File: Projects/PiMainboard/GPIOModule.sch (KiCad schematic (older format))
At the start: 0 parts

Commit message: Added lots more to modules!
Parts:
- added C1_G: 2.2pF, symbol cap_np
- added C2_G: 10pF, symbol cap_np
- added J1_G, J2_G, J3_G, J4_G: HEADER_4, symbol HEADER_4
- added J5_G: HEADER_6, symbol HEADER_6
- added R1_G, R2_G, R3_G, R4_G: 1k8, symbol R
- added R5_G: 1k, symbol R
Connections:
- net FM: now also C1_G.1, C2_G.1
- net GPIO17: now also J5_G.1
- net GPIO22: now also J5_G.2
- net GPIO23: now also J5_G.3
- net GPIO24: now also J5_G.4
- net PWM: now also J5_G.5
- net SCL: now also J1_G.2, J2_G.2, R2_G.2, R4_G.2
- net SDA: now also J1_G.1, J2_G.1, R1_G.2, R3_G.2
- net UART_RX0: now also J3_G.2
- net UART_RX1: now also J4_G.2
- net UART_TX0: now also J3_G.1
- net UART_TX1: now also J4_G.1
- new net: C1_G.2, J5_G.6, R5_G.1
- new net: C2_G.2, R5_G.2
- new net 3v3: J1_G.4, J2_G.4, J3_G.4, J4_G.4, R1_G.1, R2_G.1, R3_G.1, R4_G.1
- new net GND: J1_G.3, J2_G.3, J3_G.3, J4_G.3

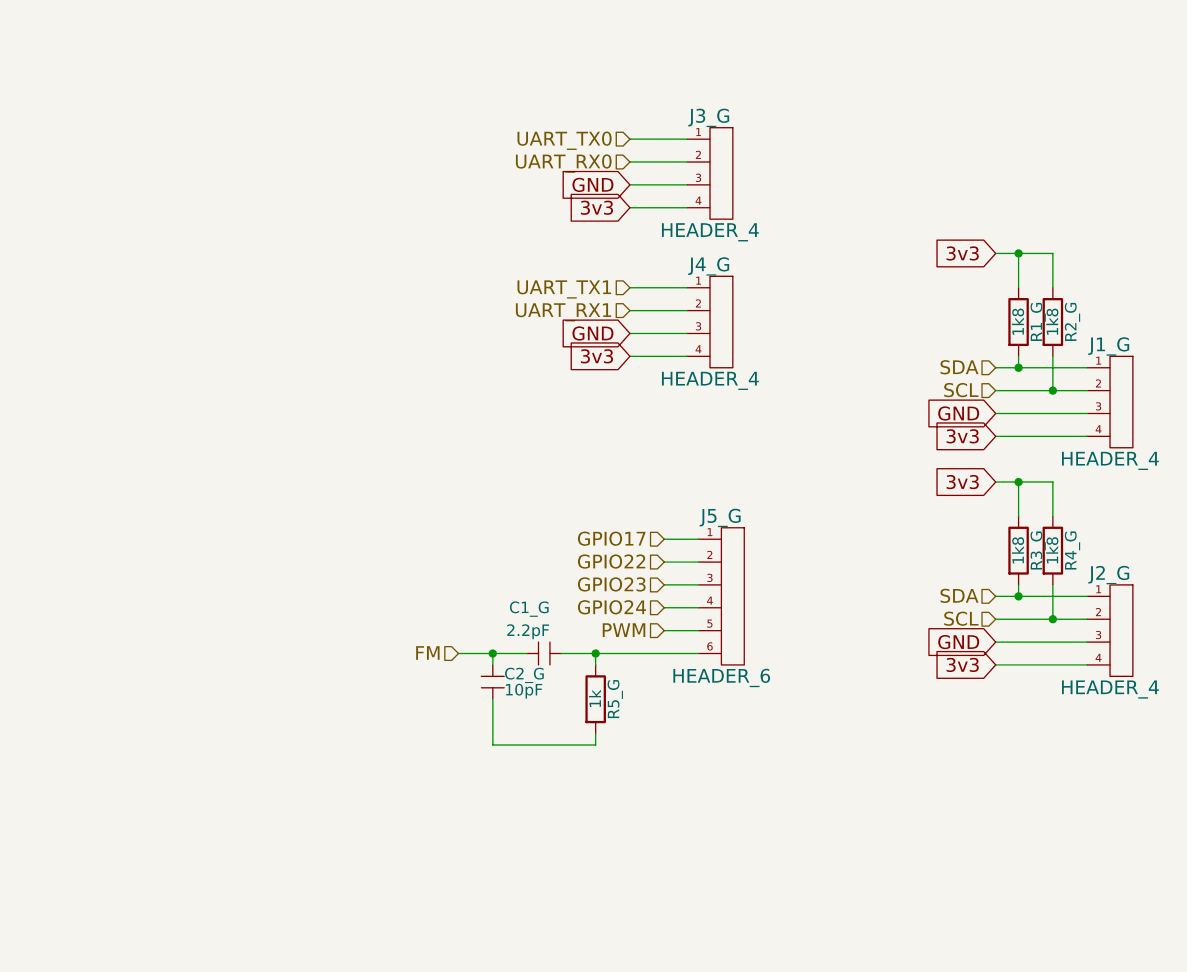
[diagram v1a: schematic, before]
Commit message: Added PI CM IO "shield"
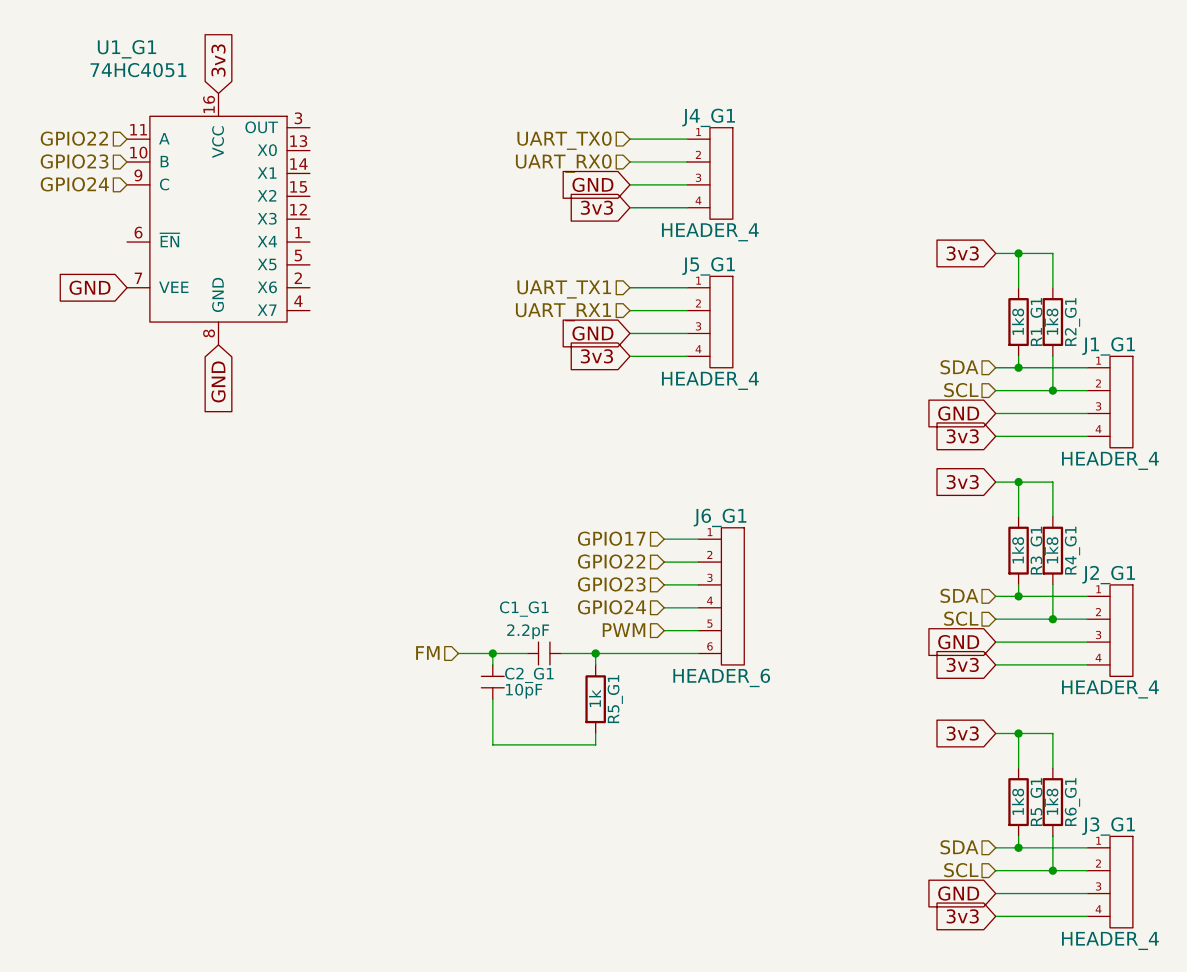
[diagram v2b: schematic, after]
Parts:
- added J3_G1: HEADER_4, symbol HEADER_4
- added R5_G1, R6_G1: 1k8, symbol R
- added U1_G1: 74HC4051, symbol 74HC4051
- renumbered C1_G to C1_G1, C2_G to C2_G1, J1_G to J1_G1, J2_G to J2_G1, J3_G to J3_G1, J4_G to J4_G1, J5_G to J5_G1, R1_G to R1_G1, R2_G to R2_G1, R3_G to R3_G1, R4_G to R4_G1, R5_G to R5_G1
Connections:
- net 3v3: now also J3_G1.4, R5_G1.1, R6_G1.1, U1_G1.16 (VCC)
- net GND: now also J3_G1.3, U1_G1.7 (VEE), U1_G1.8 (GND)
- net GPIO22: now also U1_G1.11 (A)
- net GPIO23: now also U1_G1.10 (B)
- net GPIO24: now also U1_G1.9 (C)
- net SCL: now also J3_G1.2, R6_G1.2
- net SDA: now also J3_G1.1, R5_G1.2
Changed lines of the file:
@@
 $Descr A4 11693 8268
 encoding utf-8
-Sheet 4 7
+Sheet 10 10
 Title ""
 Date ""
@@
 FM
 $Comp
-L HEADER_4 J1_G
+L HEADER_4 J1_G1
 U 1 1 5692992D
 P 6850 3000
-F 0 "J1_G" H 6850 3250 60  0000 C CNN
+AR Path="/5671AC37/5692992D" Ref="J1_G1"  Part="1"
+AR Path="/56EDDFF0/56EF4FDE/5692992D" Ref="J1_G1"  Part="1"
+F 0 "J1_G1" H 6850 3250 60  0000 C CNN
 F 1 "HEADER_4" H 6850 2750 60  0000 C CNN
 F 2 "" H 6850 3000 60  0000 C CNN
@@
 $EndComp
 $Comp
-L R R1_G
+L R R1_G1
 U 1 1 56929B23
 P 6450 2650
-F 0 "R1_G" V 6530 2650 50  0000 C CNN
+AR Path="/5671AC37/56929B23" Ref="R1_G1"  Part="1"
+AR Path="/56EDDFF0/56EF4FDE/56929B23" Ref="R1_G1"  Part="1"
+F 0 "R1_G1" V 6530 2650 50  0000 C CNN
 F 1 "1k8" V 6450 2650 50  0000 C CNN
 F 2 "" V 6380 2650 50  0000 C CNN
@@
 $EndComp
 $Comp
-L R R2_G
+L R R2_G1
 U 1 1 56929B6C
 P 6600 2650
-F 0 "R2_G" V 6680 2650 50  0000 C CNN
+AR Path="/5671AC37/56929B6C" Ref="R2_G1"  Part="1"
+AR Path="/56EDDFF0/56EF4FDE/56929B6C" Ref="R2_G1"  Part="1"
+F 0 "R2_G1" V 6680 2650 50  0000 C CNN
 F 1 "1k8" V 6600 2650 50  0000 C CNN
 F 2 "" V 6530 2650 50  0000 C CNN
@@
 SCL
 $Comp
-L HEADER_4 J2_G
+L HEADER_4 J2_G1
 U 1 1 56929E64
 P 6850 4000
-F 0 "J2_G" H 6850 4250 60  0000 C CNN
+AR Path="/5671AC37/56929E64" Ref="J2_G1"  Part="1"
+AR Path="/56EDDFF0/56EF4FDE/56929E64" Ref="J2_G1"  Part="1"
+F 0 "J2_G1" H 6850 4250 60  0000 C CNN
 F 1 "HEADER_4" H 6850 3750 60  0000 C CNN
 F 2 "" H 6850 4000 60  0000 C CNN
@@
 $EndComp
 $Comp
-L R R3_G
+L R R3_G1
 U 1 1 56929E6A
 P 6450 3650
-F 0 "R3_G" V 6530 3650 50  0000 C CNN
+AR Path="/5671AC37/56929E6A" Ref="R3_G1"  Part="1"
+AR Path="/56EDDFF0/56EF4FDE/56929E6A" Ref="R3_G1"  Part="1"
+F 0 "R3_G1" V 6530 3650 50  0000 C CNN
 F 1 "1k8" V 6450 3650 50  0000 C CNN
 F 2 "" V 6380 3650 50  0000 C CNN
@@
 $EndComp
 $Comp
-L R R4_G
+L R R4_G1
 U 1 1 56929E70
 P 6600 3650
-F 0 "R4_G" V 6680 3650 50  0000 C CNN
+AR Path="/5671AC37/56929E70" Ref="R4_G1"  Part="1"
+AR Path="/56EDDFF0/56EF4FDE/56929E70" Ref="R4_G1"  Part="1"
+F 0 "R4_G1" V 6680 3650 50  0000 C CNN
 F 1 "1k8" V 6600 3650 50  0000 C CNN
 F 2 "" V 6530 3650 50  0000 C CNN
@@
 3v3
 $Comp
-L HEADER_4 J3_G
+L HEADER_4 J3_G1
 U 1 1 5692A3DF
 P 5100 2000
-F 0 "J3_G" H 5100 2250 60  0000 C CNN
+AR Path="/5671AC37/5692A3DF" Ref="J3_G1"  Part="1"
+AR Path="/56EDDFF0/56EF4FDE/5692A3DF" Ref="J4_G1"  Part="1"
+F 0 "J4_G1" H 5100 2250 60  0000 C CNN
 F 1 "HEADER_4" H 5100 1750 60  0000 C CNN
 F 2 "" H 5100 2000 60  0000 C CNN
@@
 $EndComp
 $Comp
-L HEADER_4 J4_G
+L HEADER_4 J4_G1
 U 1 1 5692A48D
 P 5100 2650
-F 0 "J4_G" H 5100 2900 60  0000 C CNN
+AR Path="/5671AC37/5692A48D" Ref="J4_G1"  Part="1"
+AR Path="/56EDDFF0/56EF4FDE/5692A48D" Ref="J5_G1"  Part="1"
+F 0 "J5_G1" H 5100 2900 60  0000 C CNN
 F 1 "HEADER_4" H 5100 2400 60  0000 C CNN
 F 2 "" H 5100 2650 60  0000 C CNN
@@
 3v3
 $Comp
-L HEADER_6 J5_G
+L HEADER_6 J5_G1
 U 1 1 5692D1AF
 P 5150 3850
-F 0 "J5_G" H 5150 4200 60  0000 C CNN
+AR Path="/5671AC37/5692D1AF" Ref="J5_G1"  Part="1"
+AR Path="/56EDDFF0/56EF4FDE/5692D1AF" Ref="J6_G1"  Part="1"
+F 0 "J6_G1" H 5150 4200 60  0000 C CNN
 F 1 "HEADER_6" H 5150 3500 60  0000 C CNN
 F 2 "" H 5150 3850 60  0000 C CNN
@@
 $EndComp
 $Comp
-L cap_np C2_G
+L cap_np C2_G1
 U 1 1 5692D49F
 P 4150 4200
-F 0 "C2_G" H 4200 4210 50  0000 L CNN
+AR Path="/5671AC37/5692D49F" Ref="C2_G1"  Part="1"
+AR Path="/56EDDFF0/56EF4FDE/5692D49F" Ref="C2_G1"  Part="1"
+F 0 "C2_G1" H 4200 4210 50  0000 L CNN
 F 1 "10pF" H 4200 4140 50  0000 L CNN
 F 2 "" H 4150 4200 60  0000 C CNN
@@
 $EndComp
 $Comp
-L cap_np C1_G
+L cap_np C1_G1
 U 1 1 5692D596
 P 4350 4100
-F 0 "C1_G" V 4550 4050 50  0000 L CNN
+AR Path="/5671AC37/5692D596" Ref="C1_G1"  Part="1"
+AR Path="/56EDDFF0/56EF4FDE/5692D596" Ref="C1_G1"  Part="1"
+F 0 "C1_G1" V 4550 4050 50  0000 L CNN
 F 1 "2.2pF" V 4450 4050 50  0000 L CNN
 F 2 "" H 4350 4100 60  0000 C CNN
@@
 $EndComp
 $Comp
-L R R5_G
+L R R5_G1
 U 1 1 5692D5FB
 P 4600 4300
-F 0 "R5_G" V 4680 4300 50  0000 C CNN
+AR Path="/5671AC37/5692D5FB" Ref="R5_G1"  Part="1"
+AR Path="/56EDDFF0/56EF4FDE/5692D5FB" Ref="R5_G1"  Part="1"
+F 0 "R5_G1" V 4680 4300 50  0000 C CNN
 F 1 "1k" V 4600 4300 50  0000 C CNN
 F 2 "" V 4530 4300 50  0000 C CNN
@@
 Connection ~ 4150 4100
 Connection ~ 4600 4100
+Text HLabel 6350 4950 0    60   Input ~ 0
+SDA
+Text HLabel 6350 5050 0    60   Input ~ 0
+SCL
+$Comp
+L HEADER_4 J3_G1
+U 1 1 56EF8CFB
+P 6850 5100
+F 0 "J3_G1" H 6850 5350 60  0000 C CNN
+F 1 "HEADER_4" H 6850 4850 60  0000 C CNN
+F 2 "" H 6850 5100 60  0000 C CNN
+F 3 "" H 6850 5100 60  0000 C CNN
+	1    6850 5100
+	1    0    0    -1
+$EndComp
+$Comp
+L R R5_G1
+U 1 1 56EF8D01
+P 6450 4750
+F 0 "R5_G1" V 6530 4750 50  0000 C CNN
+F 1 "1k8" V 6450 4750 50  0000 C CNN
+F 2 "" V 6380 4750 50  0000 C CNN
+F 3 "" H 6450 4750 50  0000 C CNN
+	1    6450 4750
+	1    0    0    -1
+$EndComp
+$Comp
+L R R6_G1
+U 1 1 56EF8D07
+P 6600 4750
+F 0 "R6_G1" V 6680 4750 50  0000 C CNN
+F 1 "1k8" V 6600 4750 50  0000 C CNN
+F 2 "" V 6530 4750 50  0000 C CNN
+F 3 "" H 6600 4750 50  0000 C CNN
+	1    6600 4750
+	1    0    0    -1
+$EndComp
+Text GLabel 6350 5250 0    60   Input ~ 0
+3v3
+Text GLabel 6350 5150 0    60   Input ~ 0
+GND
+Text GLabel 6350 4450 0    60   Input ~ 0
+3v3
+Wire Wire Line
+	6350 4950 6750 4950
+Wire Wire Line
+	6450 4950 6450 4900
+Connection ~ 6450 4950
+Wire Wire Line
+	6600 4900 6600 5050
+Wire Wire Line
+	6350 5050 6750 5050
+Connection ~ 6600 5050
+Wire Wire Line
+	6350 5150 6750 5150
+Wire Wire Line
+	6350 5250 6750 5250
+Wire Wire Line
+	6450 4600 6450 4450
+Wire Wire Line
+	6350 4450 6600 4450
+Wire Wire Line
+	6600 4450 6600 4600
+Connection ~ 6450 4450
+$Comp
+L 74HC4051 U1_G1
+U 1 1 56EF92AF
+P 2950 2200
+F 0 "U1_G1" H 2550 2950 60  0000 C CNN
+F 1 "74HC4051" H 2600 2850 60  0000 C CNN
+F 2 "" H 2950 2200 60  0000 C CNN
+F 3 "" H 2950 2200 60  0000 C CNN
+	1    2950 2200
+	1    0    0    -1
+$EndComp
+Text GLabel 2950 2750 3    60   Input ~ 0
+GND
+Text GLabel 2950 1650 1    60   Input ~ 0
+3v3
+Text GLabel 2550 2500 0    60   Input ~ 0
+GND
+Text HLabel 2550 1850 0    60   Input ~ 0
+GPIO22
+Text HLabel 2550 1950 0    60   Input ~ 0
+GPIO23
+Text HLabel 2550 2050 0    60   Input ~ 0
+GPIO24
 $EndSCHEMATC
